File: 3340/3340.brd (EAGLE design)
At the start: 42.5 x 216.2 mm, 74 parts, among them IC2 CEM3340, Q1 2N3906, X1 2516-

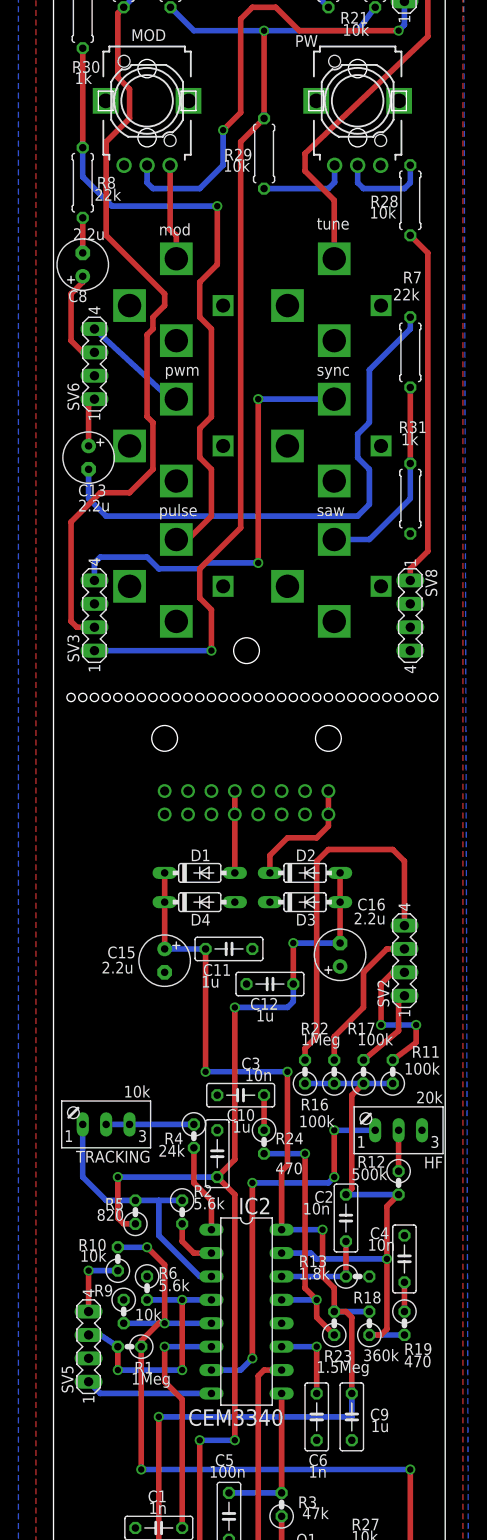
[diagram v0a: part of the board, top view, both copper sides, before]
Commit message: fixed the levels for the 3340 and vcf3
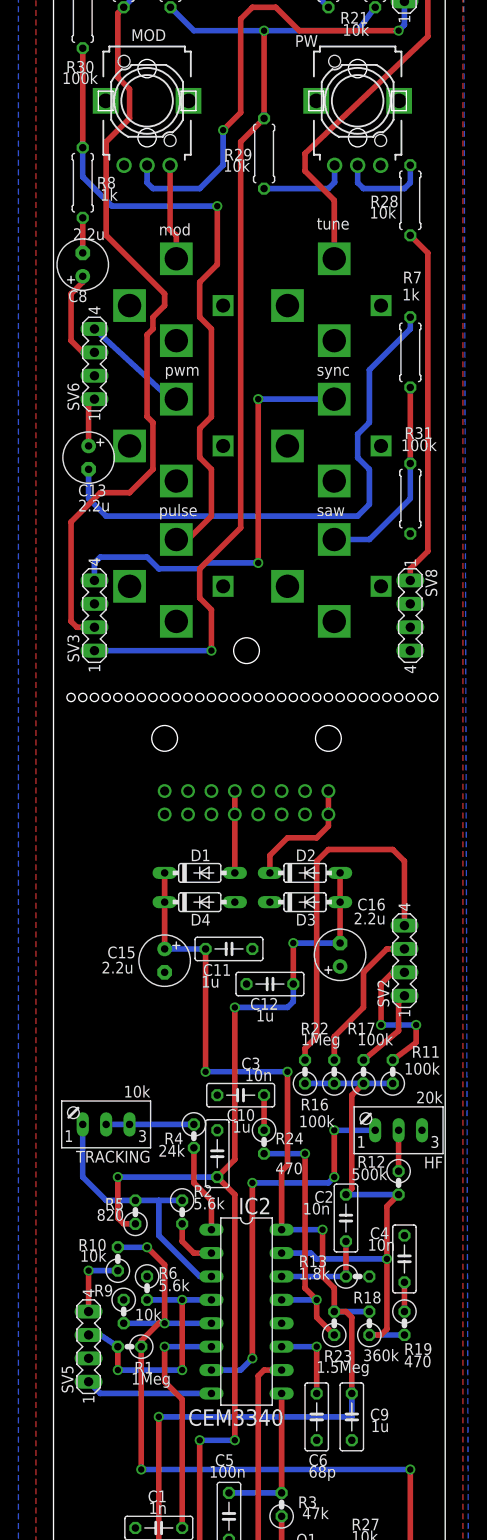
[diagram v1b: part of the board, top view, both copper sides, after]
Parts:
- C6: value 1n -> 68p
- R30, R31: value 1k -> 100k
- R7, R8: value 22k -> 1k
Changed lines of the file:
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@@
 <attribute name="VALUE" x="13.97" y="185.3692" size="1.27" layer="21" font="vector" ratio="15"/>
 </element>
-<element name="R8" library="dan" package="0207/7" value="22k" x="3.175" y="163.83" smashed="yes" rot="R270">
+<element name="R8" library="dan" package="0207/7" value="1k" x="3.175" y="163.83" smashed="yes" rot="R270">
 <attribute name="NAME" x="4.699" y="163.195" size="1.27" layer="21" font="vector" ratio="15"/>
-<attribute name="VALUE" x="4.445" y="161.8742" size="1.27" layer="21" font="vector" ratio="15"/>
+<attribute name="VALUE" x="5.08" y="161.8742" size="1.27" layer="21" font="vector" ratio="15"/>
 </element>
 <element name="SV1" library="dan" package="MA04-1" value="" x="38.1" y="187.325" smashed="yes" rot="R90">
@@
 <attribute name="VALUE" x="12.319" y="20.574" size="1.27" layer="21" font="vector" ratio="15" rot="R180"/>
 </element>
-<element name="R7" library="dan" package="0207/7" value="22k" x="38.735" y="145.415" smashed="yes" rot="R90">
+<element name="R7" library="dan" package="0207/7" value="1k" x="38.735" y="145.415" smashed="yes" rot="R90">
 <attribute name="NAME" x="40.005" y="154.178" size="1.27" layer="21" font="vector" ratio="15" rot="R180"/>
 <attribute name="VALUE" x="39.751" y="152.3238" size="1.27" layer="21" font="vector" ratio="15" rot="R180"/>
@@
 </element>
 <element name="SYNC" library="dan" package="PJ301BM" value="PJ301BM" x="30.48" y="135.255" smashed="yes"/>
-<element name="C6" library="dan" package="C050-025X075" value="1n" x="28.575" y="29.845" smashed="yes" rot="R270">
+<element name="C6" library="dan" package="C050-025X075" value="68p" x="28.575" y="29.845" smashed="yes" rot="R270">
 <attribute name="NAME" x="27.686" y="24.511" size="1.27" layer="21" font="vector" ratio="15"/>
 <attribute name="VALUE" x="27.686" y="23.241" size="1.27" layer="21" font="vector" ratio="15"/>
@@
 <attribute name="VALUE" x="21.336" y="166.2938" size="1.27" layer="21" font="vector" ratio="15" rot="R180"/>
 </element>
-<element name="R30" library="dan" package="0207/7" value="1k" x="3.175" y="182.245" smashed="yes" rot="R90">
-<attribute name="NAME" x="5.08" y="177.038" size="1.27" layer="21" font="vector" ratio="15" rot="R180"/>
-<attribute name="VALUE" x="4.191" y="175.8188" size="1.27" layer="21" font="vector" ratio="15" rot="R180"/>
-</element>
-<element name="R31" library="dan" package="0207/7" value="1k" x="38.735" y="129.54" smashed="yes" rot="R270">
-<attribute name="NAME" x="37.465" y="136.652" size="1.27" layer="21" font="vector" ratio="15"/>
-<attribute name="VALUE" x="37.719" y="135.3312" size="1.27" layer="21" font="vector" ratio="15"/>
+<element name="R30" library="dan" package="0207/7" value="100k" x="3.175" y="182.245" smashed="yes" rot="R90">
+<attribute name="NAME" x="4.445" y="177.038" size="1.27" layer="21" font="vector" ratio="15" rot="R180"/>
+<attribute name="VALUE" x="4.826" y="175.8188" size="1.27" layer="21" font="vector" ratio="15" rot="R180"/>
+</element>
+<element name="R31" library="dan" package="0207/7" value="100k" x="38.735" y="129.54" smashed="yes" rot="R270">
+<attribute name="NAME" x="38.1" y="136.017" size="1.27" layer="21" font="vector" ratio="15"/>
+<attribute name="VALUE" x="37.719" y="134.6962" size="1.27" layer="21" font="vector" ratio="15"/>
 </element>
 <element name="C8" library="dan" package="E2,5-6" value="2.2u" x="3.175" y="154.94" smashed="yes" rot="R90">

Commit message: added state variable filter, changed pw resistor on vco
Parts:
- R29: value 10k -> 1k
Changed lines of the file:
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@@
 <attribute name="VALUE" x="37.211" y="161.2138" size="1.27" layer="21" font="vector" ratio="15" rot="R180"/>
 </element>
-<element name="R29" library="dan" package="0207/7" value="10k" x="22.86" y="167.005" smashed="yes" rot="R90">
+<element name="R29" library="dan" package="0207/7" value="1k" x="22.86" y="167.005" smashed="yes" rot="R90">
 <attribute name="NAME" x="21.59" y="167.513" size="1.27" layer="21" font="vector" ratio="15" rot="R180"/>
 <attribute name="VALUE" x="21.336" y="166.2938" size="1.27" layer="21" font="vector" ratio="15" rot="R180"/>

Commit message: added tri and linear mod to vco, fixed serious errors with cvsource
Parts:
- removed SV1, SV2: (no value), dan:MA04-1
- added C17: 10n, dan:C050-025X075
- added C18: 2.2u, dan:E2,5-6
- added CVIN2, SAW1: PJ301BM, dan:PJ301BM
- added JP1, JP2: (no value), dan:1X06
- added MOD1: US-EVUF2J, dan:EVUFXJ
- added R32: 1Meg, dan:0207/2V
- added R33: 1k, dan:0207/7
- added R34: 100k, dan:0207/7
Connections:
- new net N$24: C17.1, R32.1
- new net N$51: C17.2, JP1.6
- new net N$52: JP2.6, MOD1.2
- new net N$53: C18.+, R33.2
- new net N$54: R33.1, R34.1, SAW1.P$3
- new net N$55: C18.-, JP2.5
- new net N$56: CVIN2.P$3, MOD1.3
- net GND: now also CVIN2.P$1, CVIN2.P$2, CVIN2.P$4, MOD1.1, R34.2, SAW1.P$1, SAW1.P$4
- net N$17: now also JP1.4; no longer SV2.4
- net N$21: now also JP1.1; no longer SV2.1
- net N$25: now also JP1.2; no longer SV2.2
- net N$31: now also JP2.1; no longer SV1.1
- net N$32: now also JP1.5
- net N$35: now also JP2.2; no longer SV1.2
- net N$37: now also JP2.3; no longer SV1.3
- net N$38: now also R32.2
- net N$39: now also JP1.3; no longer SV2.3
- net N$5: now also JP2.4; no longer SV1.4
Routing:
- net N$5: track 72.7 -> 11.3 mm, vias 4 -> 2
- net N$35: track 39.7 -> 31.2 mm
- net N$17: track 39.7 -> 32.7 mm
- net N$31: track 50.3 -> 47.7 mm
- net N$39: track 16.3 -> 14.4 mm
- net N$25: track 16.4 -> 15.1 mm
- net N$37: track 12.8 -> 11.6 mm
- net N$21: track 9.03 -> 8.13 mm
